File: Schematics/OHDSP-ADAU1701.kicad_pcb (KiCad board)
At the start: 4 copper layers, 100 x 100 mm, 272 parts, among them CN401 COAX, CN402 COAX, P201 CONN_2x1, P301 PIN, P302 PIN, P303 PIN, P305 CONN_2x1, P306 PIN, P501 CONN_02X10, P502 CONN_02X05, P503 CONN_02X05, P504 CONN_02X05, P505 CONN_02X10, P506 CONN_2x1, P507 CONN_2x1, P508 CONN_02X20, P509 CONN_02X05, P510 CONN_02X05, P511 CONN_02X05, P512 CONN_2x1, P513 CONN_2x1, P514 CONN_2x1, P515 CONN_2x1, SW201 SWITCH, U201 ADM13307-5ARZ, U202 ADAU1701JSTZ, U203 IC-EEPROM-I2C, U301 LT1374CS8-5#PBF, U302 NCP700BSN33T1G, U303 NCP700BSN33T1G, U304 NCP700BSN18T1G, U403 NB3L553

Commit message: WIP
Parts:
- moved C237 109.6 mm to (271.0, 95.6)
- moved R413 0.51 mm to (272.4, 91.9)
- moved C246 0.36 mm to (268.2, 97.9)
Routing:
- net /ADAU1701/CM: track 7.09 -> 7.97 mm
- net /ADAU1701/MCLK: track 5.01 -> 5.53 mm
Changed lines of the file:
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@@
   (general
     (links 549)
-    (no_connects 499)
+    (no_connects 501)
     (area 204.949999 23.949999 305.050001 124.050001)
     (thickness 1.6)
     (drawings 22)
-    (tracks 255)
+    (tracks 258)
     (zones 0)
     (modules 272)
@@
   )
   (module OHDSP-Footprints-Pretty:SMD-0805 (layer F.Cu)
-    (at 272.415 92.456 90)
+    (at 272.415 91.948 90)
     (attr smd)
     (fp_text reference R413 (at 0.254 -1.524 90) (layer F.SilkS)
@@
   )
   (module OHDSP-Footprints-Pretty:SMD-0805 (layer F.Cu)
-    (at 211.159952 187.466 270)
+    (at 271.018 95.631 270)
     (attr smd)
     (fp_text reference C237 (at 0.254 -1.524 270) (layer F.SilkS)
@@
   )
   (module OHDSP-Footprints-Pretty:SMD-0805 (layer F.Cu)
-    (at 268.478 97.663 270)
+    (at 268.224 97.917 270)
     (attr smd)
     (fp_text reference C246 (at 0.254 -1.524 270) (layer F.SilkS)
@@
   (segment (start 266.192 106.172) (end 267.244 105.12) (width 0.2) (layer F.Cu) (net 116))
   (segment (start 268.7 105.12) (end 267.244 105.12) (width 0.2) (layer F.Cu) (net 116))
-  (segment (start 259.582883 98.165883) (end 261.366 99.949) (width 0.3) (layer F.Cu) (net 117))
+  (segment (start 258.947883 98.546883) (end 260.35 99.949) (width 0.3) (layer F.Cu) (net 117))
+  (segment (start 260.35 99.949) (end 262.636 99.949) (width 0.3) (layer F.Cu) (net 117))
   (segment (start 263.017 99.949) (end 263.017 99.929) (width 0.3) (layer F.Cu) (net 117))
-  (segment (start 261.366 99.949) (end 263.017 99.949) (width 0.3) (layer F.Cu) (net 117))
+  (segment (start 262.636 99.949) (end 263.017 99.949) (width 0.3) (layer F.Cu) (net 117))
   (segment (start 268.7 102.12) (end 266.966 102.12) (width 0.3) (layer F.Cu) (net 117))
   (segment (start 264.541 99.949) (end 264.541 99.929) (width 0.3) (layer F.Cu) (net 117))
@@
   (segment (start 266.966 102.12) (end 264.795 99.949) (width 0.3) (layer F.Cu) (net 117))
   (segment (start 264.541 99.929) (end 263.017 99.929) (width 0.3) (layer F.Cu) (net 117))
-  (segment (start 266.7635 100.9015) (end 265.049 99.187) (width 0.3) (layer F.Cu) (net 118))
-  (segment (start 265.049 99.187) (end 265.049 96.754) (width 0.3) (layer F.Cu) (net 118) (status 800000))
+  (segment (start 264.16 96.246) (end 264.16 98.298) (width 0.3) (layer F.Cu) (net 118))
+  (segment (start 264.16 98.298) (end 265.303 99.441) (width 0.3) (layer F.Cu) (net 118))
+  (segment (start 266.7635 100.9015) (end 265.303 99.441) (width 0.3) (layer F.Cu) (net 118))
   (segment (start 268.7 101.62) (end 267.482 101.62) (width 0.3) (layer F.Cu) (net 118))
   (segment (start 267.482 101.62) (end 266.7635 100.9015) (width 0.3) (layer F.Cu) (net 118))
@@
   (segment (start 276.055 78.105) (end 279.4 78.105) (width 0.2) (layer F.Cu) (net 145))
   (segment (start 346.174407 52.167281) (end 346.344407 52.33728) (width 0.2) (layer F.Cu) (net 147))
-  (segment (start 272.415 93.556) (end 272.3 93.671) (width 0.2) (layer F.Cu) (net 151))
-  (segment (start 272.3 93.671) (end 272.3 98.52) (width 0.3) (layer F.Cu) (net 151))
+  (segment (start 272.3 98.52) (end 272.288 98.508) (width 0.3) (layer F.Cu) (net 151))
+  (segment (start 272.288 98.508) (end 272.288 93.175) (width 0.3) (layer F.Cu) (net 151))
+  (segment (start 272.288 93.175) (end 272.415 93.048) (width 0.3) (layer F.Cu) (net 151))
   (segment (start 277.4 101.62) (end 281.706 101.62) (width 0.2) (layer F.Cu) (net 160))
   (segment (start 289.39 104.14) (end 290.957 102.573) (width 0.2) (layer F.Cu) (net 160))

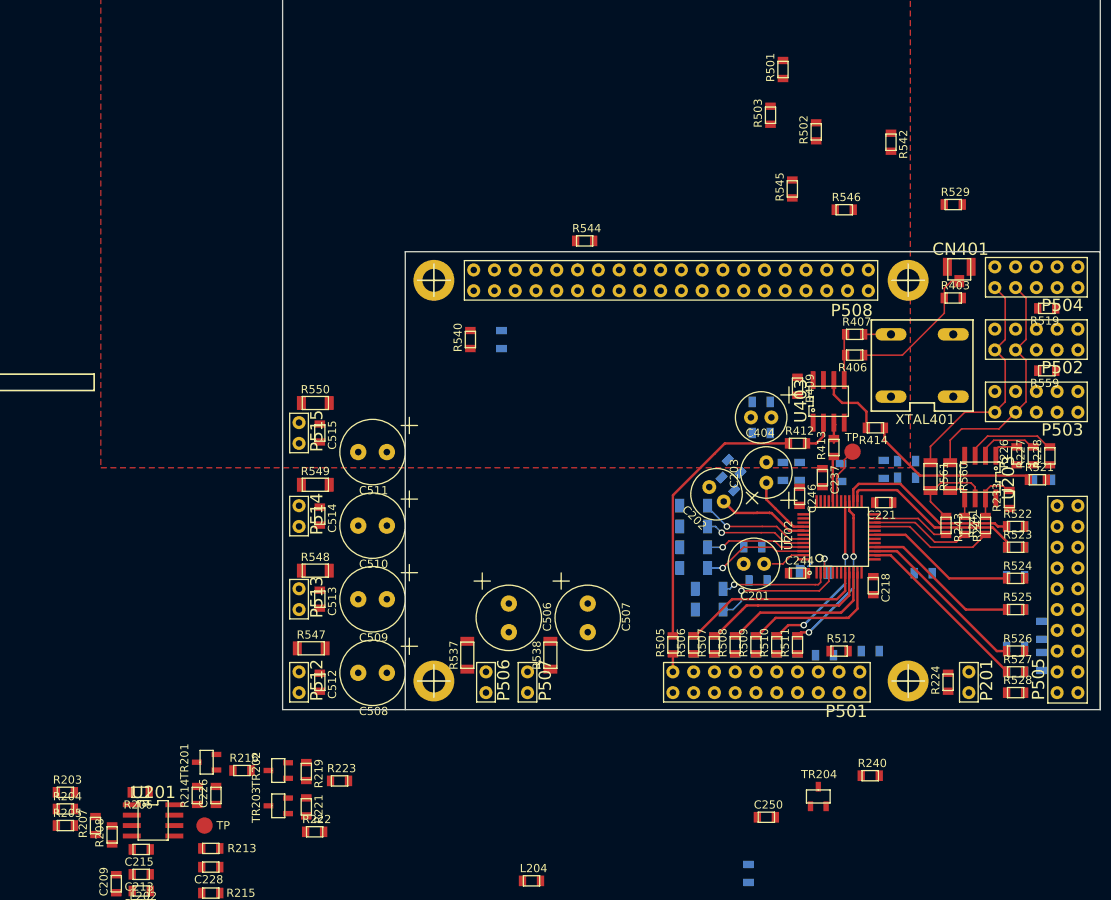
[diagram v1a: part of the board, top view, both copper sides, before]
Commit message: Change reset chip to ADM811
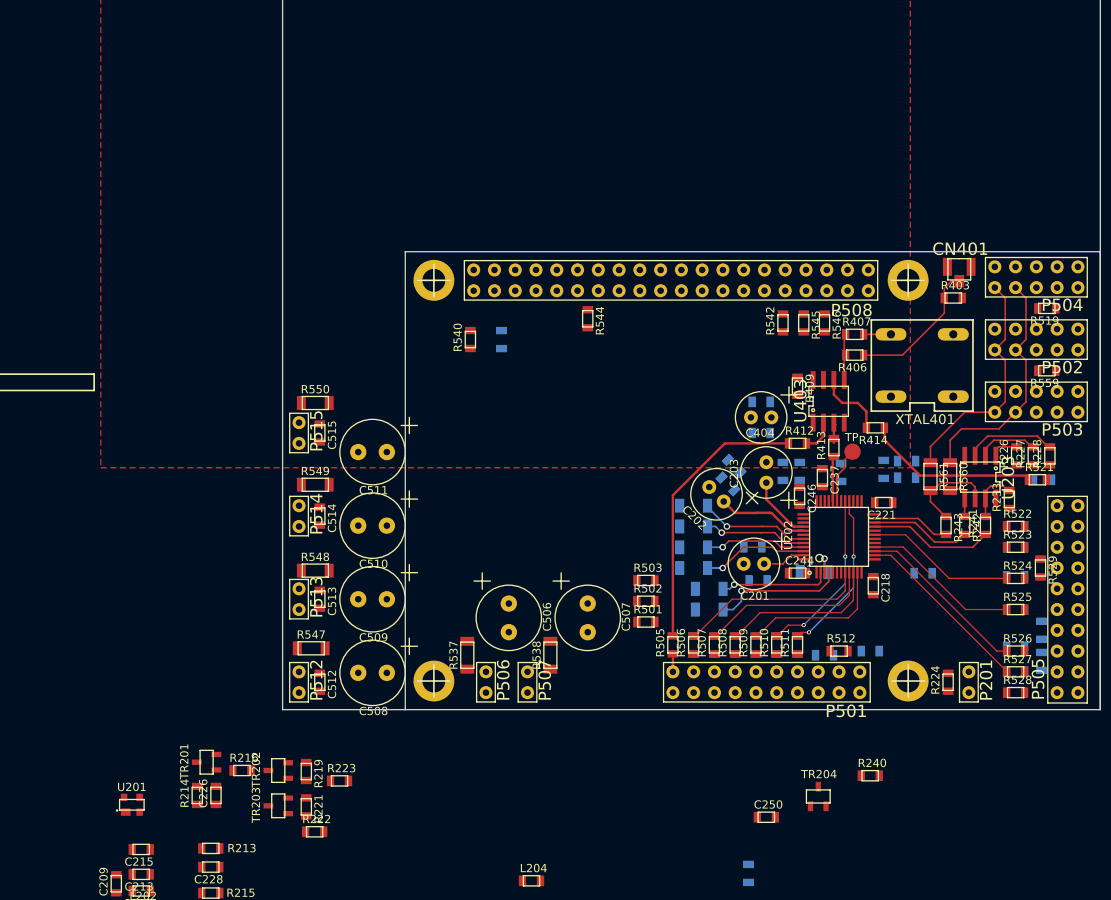
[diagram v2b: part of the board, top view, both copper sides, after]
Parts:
- removed R203: 0R, OHDSP-Footprints-Pretty:SMD-0805
- removed R204: 12k, OHDSP-Footprints-Pretty:SMD-0805
- removed R205: 8k2, OHDSP-Footprints-Pretty:SMD-0805
- removed R206: N/F, OHDSP-Footprints-Pretty:SMD-0805
- removed R207: 3k, OHDSP-Footprints-Pretty:SMD-0805
- removed R208: 4k7, OHDSP-Footprints-Pretty:SMD-0805
- removed TP202: TP, OHDSP-Footprints-Pretty:TP-2mm
- U201: value ADM13307-5ARZ -> IC-RST-ADM811; footprint OHDSP-Footprints-Pretty:IC_SOIC_8 -> OHDSP-Footprints-Pretty:IC-SOT143
- moved R501 69.6 mm to (249.4, 113.3), turned to 0 degrees
- moved R502 61.1 mm to (249.4, 110.7), turned to 0 degrees
- moved R503 58.9 mm to (249.4, 108.2), turned to 0 degrees
- moved R529 45.7 mm to (297.7, 106.7), turned to 270 degrees
- moved R542 25.7 mm to (266.2, 76.7), turned to 90 degrees
- moved R545 16.4 mm to (268.7, 76.7), turned to 270 degrees
- moved R546 14.1 mm to (271.3, 76.7), turned to 270 degrees
- moved R544 9.53 mm to (242.3, 76.2), turned to 270 degrees
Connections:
- P501 pad 16: (no net) -> Net-(P501-Pad16)
- P501 pad 20: (no net) -> Net-(P501-Pad20)
- P502 pad 2: (no net) -> Net-(P502-Pad2)
- P502 pad 4: (no net) -> Net-(P502-Pad4)
- P502 pad 5: (no net) -> Net-(P502-Pad5)
- P502 pad 7: (no net) -> Net-(P502-Pad7)
- P502 pad 8: (no net) -> Net-(P502-Pad8)
- P502 pad 9: (no net) -> Net-(P502-Pad9)
- P503 pad 2: (no net) -> Net-(P503-Pad2)
- P503 pad 4: (no net) -> Net-(P503-Pad4)
- P503 pad 5: (no net) -> Net-(P503-Pad5)
- P503 pad 7: (no net) -> Net-(P503-Pad7)
- P503 pad 8: (no net) -> Net-(P503-Pad8)
- P503 pad 9: (no net) -> Net-(P503-Pad9)
- P504 pad 2: (no net) -> Net-(P504-Pad2)
- P504 pad 4: (no net) -> Net-(P504-Pad4)
- P504 pad 5: (no net) -> Net-(P504-Pad5)
- P504 pad 7: (no net) -> Net-(P504-Pad7)
- P504 pad 8: (no net) -> Net-(P504-Pad8)
- P504 pad 9: (no net) -> Net-(P504-Pad9)
- P505 pad 15: (no net) -> Net-(P505-Pad15)
- P505 pad 19: (no net) -> Net-(P505-Pad19)
- P508 pad 1: (no net) -> Net-(P508-Pad1)
- P508 pad 17: (no net) -> Net-(P508-Pad17)
- U201 pad 1: Net-(R203-Pad2) -> GNDD
- U201 pad 2: Net-(R204-Pad2) -> Net-(R213-Pad1)
- U201 pad 3: Net-(R205-Pad2) -> Net-(C226-Pad1)
- U201 pad 4: GNDD -> Net-(C213-Pad1)
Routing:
- net /ADAU1701/DACOUT_SDATA2: track 43.5 -> 0.34 mm
- net /ADAU1701/DACOUT_SDATA3: track 3.12 -> 0.86 mm
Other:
- rule trace_min: 0.2 -> 0.15
- board text added: "Dirty PCB 4 layer stackup: 1oz copper 0.2mm FR5 0.5oz copper 1.2mm FR4 0.5oz copper 0.2mm FR4 1oz copper 50ohm traces with ground plane: Trace 0.35mm, Clearance 0.2mm 75ohm traces with ground plane: Trace 0.2mm, Clearance 0.3mm 89ohm traces with ground plane: Trace 0.15mm, Clearance 0.5mm (Use 26AWG ribbon cables)"
- board text removed: "Seeed Studio/Fusion PCB do a 1mm stackup that would give reasonable trace widths For 50ohm on top use inner top layer as ground (5mil thick) Trace width is 0.24mm, ground clearance anything <1mm For 75ohm on top use inner bottom layer as ground (29mil thick) Trace width is 0.5mm with ground on 0.4mm clearance OR Trace width is 0.45mm with ground on 0.3mm clearance For 90ohm on top use inner botto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"

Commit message: Change to box headers
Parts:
- P501, P505: footprint OHDSP-Footprints-Pretty:CONN_DIL_2X10 -> OHDSP-Footprints-Pretty:CONN_DIL_2X10_BOX
- P502, P503, P504: footprint OHDSP-Footprints-Pretty:CONN_DIL_2X5 -> OHDSP-Footprints-Pretty:CONN_DIL_2X5_BOX
- moved P503 35.3 mm to (279.4, 55.9), turned to 0 degrees
- moved P502 24.1 mm to (289.6, 55.9), turned to 0 degrees
- moved P505 16.6 mm to (299.7, 106.7)
- moved P501 15.5 mm to (261.6, 118.1)
- moved P504 15.5 mm to (299.7, 55.9), turned to 0 degrees

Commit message: WIP
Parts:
- moved R517 10.7 mm to (271.3, 126.2)
- moved R518 10.5 mm to (267.0, 126.5)
- moved R516 10.5 mm to (251.2, 125.7)
- moved R520 10.4 mm to (262.6, 126.5)
- moved R514 10.3 mm to (258.8, 126.2)
- moved R515 9.98 mm to (255.3, 125.7)
- moved R501 8.95 mm to (244.3, 105.9)
- moved R502 8.95 mm to (244.3, 103.4)
- moved R503 8.95 mm to (244.3, 100.8)
- moved R506 5.45 mm to (252.7, 111.3)
- moved R508 5.45 mm to (257.8, 111.3)
- moved R510 5.45 mm to (262.9, 111.3)
- moved R511 5.45 mm to (265.4, 111.3)
- moved R505 5.45 mm to (250.2, 111.3)
- moved R507 5.45 mm to (255.3, 111.3)
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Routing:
- net /ADAU1701/ADCIN_LRCLK0: track 23.1 -> 0.00 mm
- net /ADAU1701/ADCIN_BCLK0: track 21.3 -> 0.00 mm
- net /ADAU1701/ADCIN_SDATA0: track 19.7 -> 0.00 mm
- net /ADAU1701/ADCIN_SDATA1: track 18.2 -> 0.00 mm
- net Net-(P501-Pad2): track 2.20 -> 4.49 mm
- net /Connectors/ADC_MCLK: track 34.0 -> 32.6 mm
